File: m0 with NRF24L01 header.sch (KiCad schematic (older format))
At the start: 6 parts

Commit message: Schematic complete
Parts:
- added J?: UART, symbol Connector_Generic:Conn_01x03
- added J?: I2C, symbol Connector_Generic:Conn_01x04
- added J?: ARDU_PINS, symbol Connector:Conn_01x06_Female
- added J?: ARDU_PINS_GND, symbol Connector:Conn_01x06_Female
- added J?: ARDU_PINS_3V3, symbol Connector:Conn_01x06_Female
- added J?: Extra Pins, symbol Connector:Conn_01x07_Female
- added J?: Extra Pins GND, symbol Connector:Conn_01x07_Female
- added J?: Extra Pins 3V3, symbol Connector:Conn_01x07_Female
- added Q?: Q_NMOS_DGS, symbol Device:Q_NMOS_DGS
- added R? (x2): 10k, symbol Device:R
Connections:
- net +3V3: now also J?.1 (Pin_1), J?.1 (Pin_1), J?.1 (Pin_1), J?.2 (Pin_2), J?.2 (Pin_2), J?.3 (Pin_3), J?.3 (Pin_3), J?.4 (Pin_4), J?.4 (Pin_4), J?.5 (Pin_5), J?.5 (Pin_5), J?.6 (Pin_6), J?.6 (Pin_6), J?.7 (Pin_7), Q?.2 (G), R?.1
- net +BATT: now also R?.1
- net GND: now also J?.1 (Pin_1), J?.1 (Pin_1), J?.2 (Pin_2), J?.2 (Pin_2), J?.3 (Pin_3), J?.3 (Pin_3), J?.3 (Pin_3), J?.4 (Pin_4), J?.4 (Pin_4), J?.4 (Pin_4), J?.5 (Pin_5), J?.5 (Pin_5), J?.6 (Pin_6), J?.6 (Pin_6), J?.7 (Pin_7)
- net RX: now also J?.2 (Pin_2)
- net SCL: now also J?.2 (Pin_2)
- net SDA: now also J?.3 (Pin_3)
- net TX: now also J?.1 (Pin_1)
- net Taranis_HEARTBEAT: now also Q?.1 (D), R?.2
- net PWM_TC_INPUT: now reaches Q?.3 (S), R?.2
- new net ARDU_10: J?.2 (Pin_2)
- new net ARDU_12: J?.3 (Pin_3)
- new net ARDU_14: J?.4 (Pin_4)
- new net ARDU_15: J?.5 (Pin_5)
- new net ARDU_19: J?.6 (Pin_6)
- new net ARDU_6: J?.1 (Pin_1)
- new net PA03: J?.1 (Pin_1)
- new net PA21: J?.2 (Pin_2)
- new net PA27: J?.3 (Pin_3)
- new net PA28: J?.4 (Pin_4)
- new net PB03: J?.5 (Pin_5)
- new net PB22: J?.6 (Pin_6)
- new net PB23: J?.7 (Pin_7)
- new net Taranis_HEARTBEAT_3V3: Q?.3 (S), R?.2
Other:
- note added: "Needs to go to timer input"
- note added: "PA07:\nEXTINT[7]\nTCC1(W0)\nTCC3(WO)"
- note added: "To MCU (+VBatt)"
- note added: "To MCU (3.3V)"

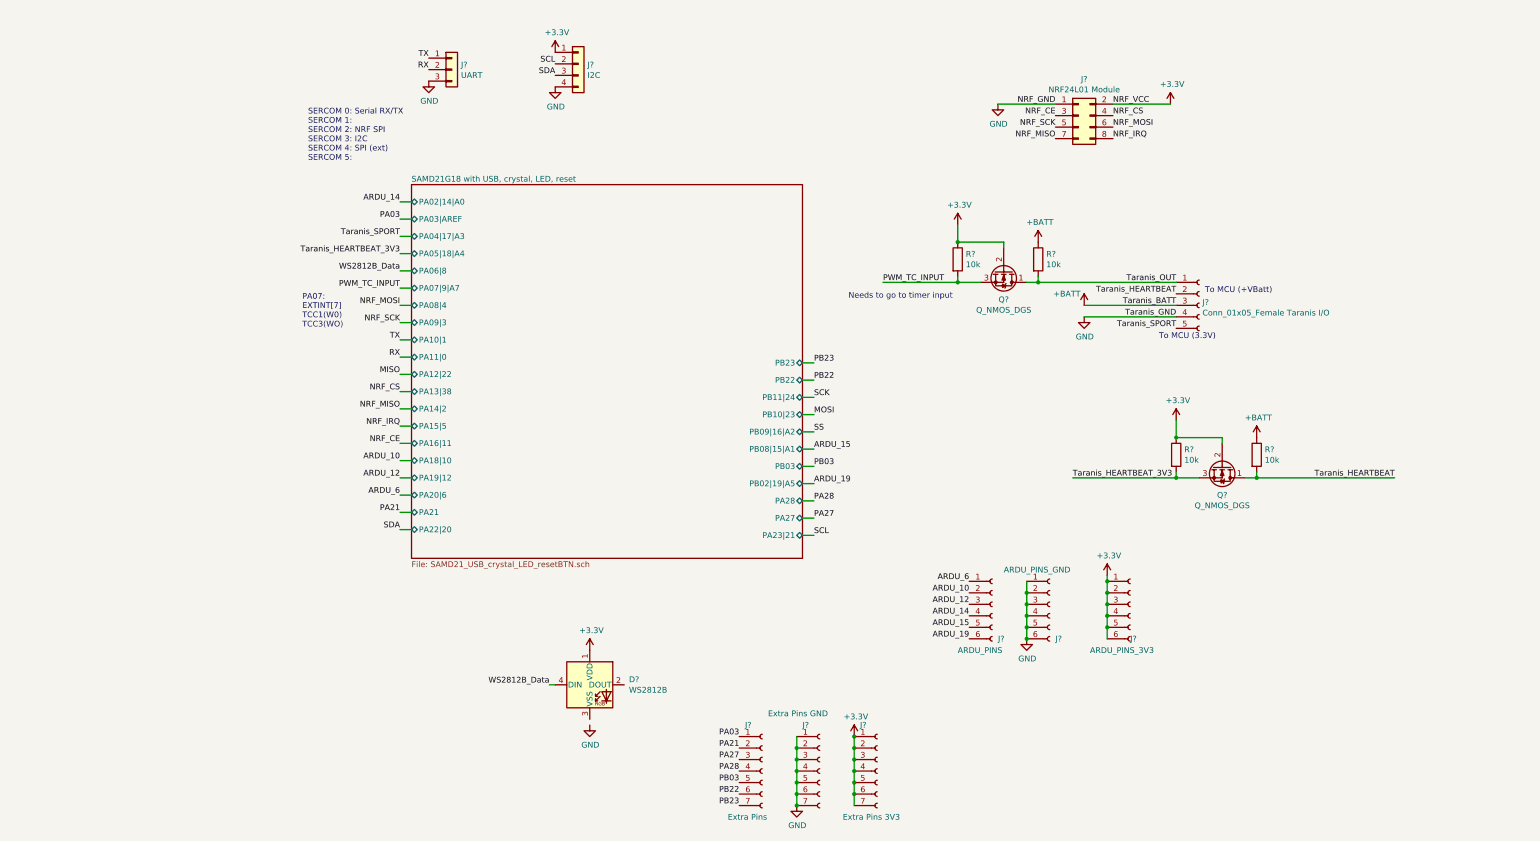
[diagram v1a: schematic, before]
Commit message: Add 3v3 LDO, annotate schematic
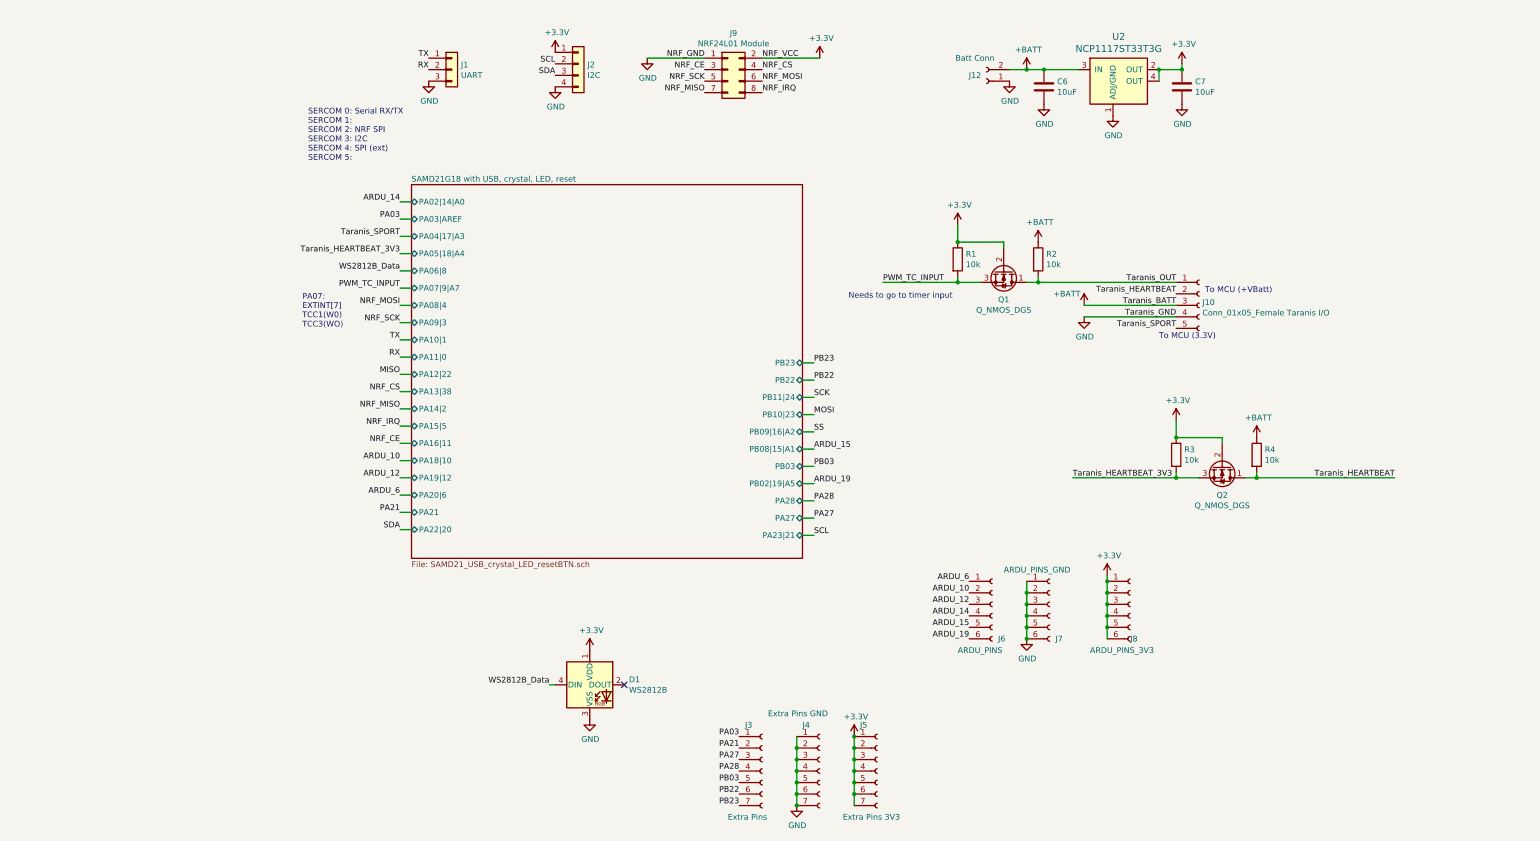
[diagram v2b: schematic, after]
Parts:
- added C6, C7: 10uF, symbol Device:C
- added J12: Batt Conn, symbol Connector:Conn_01x02_Female
- added U2: NCP1117ST33T3G, digikey-footprints:SOT-223, symbol dk_PMIC-Voltage-Regulators-Linear:NCP1117ST33T3G
- gave numbers to parts that had none: 17
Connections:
- net +3V3: now also C7.1, U2.2 (OUT), U2.4 (OUT)
- net +BATT: now also C6.1, J12.2 (Pin_2), U2.3 (IN)
- net GND: now also D1.3 (VSS), C6.2, C7.2, J12.1 (Pin_1), U2.1 (ADJ/GND)
- no-connect marks 0 -> 1
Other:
- moved on the sheet: J9

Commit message: Fix schematic ERC
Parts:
- added D3, D4: D_Schottky, symbol Device:D_Schottky
- added J13: SPI, symbol Connector:Conn_01x06_Female
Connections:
- net +3V3: now also J13.1 (Pin_1)
- net +BATT: now also D3.2 (A); no longer C6.1, U2.3 (IN)
- net GND: now also J13.6 (Pin_6)
- net MISO: now also J13.3 (Pin_3)
- net MOSI: now also J13.2 (Pin_2)
- net SCK: now also J13.4 (Pin_4)
- net SS: now also J13.5 (Pin_5)
- new net: C6.1, D3.1 (K), D4.1 (K), U2.3 (IN)
- new net +5V_USB: D4.2 (A)
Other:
- moved on the sheet: C6, C7, U2

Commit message: XCtal caps changed, all footprints assigned
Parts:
- C6: footprint (none) -> Capacitor_SMD:C_1206_3216Metric
- C7: footprint (none) -> Capacitor_SMD:C_0805_2012Metric; Part (none) -> TPSP106M010R2000
- D3, D4: footprint (none) -> Diode_SMD:D_SMC_Handsoldering
- J1: footprint (none) -> Connector_PinHeader_1.27mm:PinHeader_1x03_P1.27mm_Vertical
- J12: footprint (none) -> Connector_PinHeader_1.27mm:PinHeader_1x02_P1.27mm_Vertical
- J13, J6, J7, J8: footprint (none) -> Connector_PinHeader_1.27mm:PinHeader_1x06_P1.27mm_Vertical
- J2: footprint (none) -> Connector_PinHeader_1.27mm:PinHeader_1x04_P1.27mm_Vertical
- J3, J4, J5: footprint (none) -> Connector_PinHeader_1.27mm:PinHeader_1x07_P1.27mm_Vertical
- J9: footprint (none) -> Connector_PinHeader_1.27mm:PinHeader_2x04_P1.27mm_Vertical
- Q1, Q2: value Q_NMOS_DGS -> SI2304DDS-T1-GE3; footprint (none) -> Package_TO_SOT_SMD:SOT-23
- R1, R2, R3, R4: footprint (none) -> Resistor_SMD:R_0603_1608Metric
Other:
- note added: "ESR: 33mOhm to 2.2Ohm"
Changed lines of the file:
@@
 F 0 "J9" H 4300 1317 50  0000 C CNN
 F 1 "NRF24L01 Module" H 4300 1226 50  0000 C CNN
-F 2 "" H 4250 1000 50  0001 C CNN
+F 2 "Connector_PinHeader_1.27mm:PinHeader_2x04_P1.27mm_Vertical" H 4250 1000 50  0001 C CNN
 F 3 "~" H 4250 1000 50  0001 C CNN
 	1    4250 1000
@@
 P 6650 2750
 F 0 "Q1" V 6900 2750 50  0000 C CNN
-F 1 "Q_NMOS_DGS" V 6991 2750 50  0000 C CNN
-F 2 "" H 6850 2850 50  0001 C CNN
+F 1 "SI2304DDS-T1-GE3" V 6991 2750 50  0000 C CNN
+F 2 "Package_TO_SOT_SMD:SOT-23" H 6850 2850 50  0001 C CNN
 F 3 "~" H 6650 2750 50  0001 C CNN
 	1    6650 2750
@@
 F 0 "R2" H 7020 2696 50  0000 L CNN
 F 1 "10k" H 7020 2605 50  0000 L CNN
-F 2 "" V 6880 2650 50  0001 C CNN
+F 2 "Resistor_SMD:R_0603_1608Metric" V 6880 2650 50  0001 C CNN
 F 3 "~" H 6950 2650 50  0001 C CNN
 	1    6950 2650
@@
 F 0 "R1" H 6320 2696 50  0000 L CNN
 F 1 "10k" H 6320 2605 50  0000 L CNN
-F 2 "" V 6180 2650 50  0001 C CNN
+F 2 "Resistor_SMD:R_0603_1608Metric" V 6180 2650 50  0001 C CNN
 F 3 "~" H 6250 2650 50  0001 C CNN
 	1    6250 2650
@@
 F 0 "J2" H 3030 942 50  0000 L CNN
 F 1 "I2C" H 3030 851 50  0000 L CNN
-F 2 "" H 2950 950 50  0001 C CNN
+F 2 "Connector_PinHeader_1.27mm:PinHeader_1x04_P1.27mm_Vertical" H 2950 950 50  0001 C CNN
 F 3 "~" H 2950 950 50  0001 C CNN
 	1    2950 950
@@
 P 8550 4450
 F 0 "Q2" V 8800 4450 50  0000 C CNN
-F 1 "Q_NMOS_DGS" V 8891 4450 50  0000 C CNN
-F 2 "" H 8750 4550 50  0001 C CNN
+F 1 "SI2304DDS-T1-GE3" V 8891 4450 50  0000 C CNN
+F 2 "Package_TO_SOT_SMD:SOT-23" H 8750 4550 50  0001 C CNN
 F 3 "~" H 8550 4450 50  0001 C CNN
 	1    8550 4450
@@
 F 0 "R4" H 8920 4396 50  0000 L CNN
 F 1 "10k" H 8920 4305 50  0000 L CNN
-F 2 "" V 8780 4350 50  0001 C CNN
+F 2 "Resistor_SMD:R_0603_1608Metric" V 8780 4350 50  0001 C CNN
 F 3 "~" H 8850 4350 50  0001 C CNN
 	1    8850 4350
@@
 F 0 "R3" H 8220 4396 50  0000 L CNN
 F 1 "10k" H 8220 4305 50  0000 L CNN
-F 2 "" V 8080 4350 50  0001 C CNN
+F 2 "Resistor_SMD:R_0603_1608Metric" V 8080 4350 50  0001 C CNN
 F 3 "~" H 8150 4350 50  0001 C CNN
 	1    8150 4350
@@
 F 0 "J6" H 6600 5350 50  0000 L CNN
 F 1 "ARDU_PINS" H 6250 5250 50  0000 L CNN
-F 2 "" H 6550 5650 50  0001 C CNN
+F 2 "Connector_PinHeader_1.27mm:PinHeader_1x06_P1.27mm_Vertical" H 6550 5650 50  0001 C CNN
 F 3 "~" H 6550 5650 50  0001 C CNN
 	1    6550 5650
@@
 F 0 "J7" H 7100 5350 50  0000 L CNN
 F 1 "ARDU_PINS_GND" H 6650 5950 50  0000 L CNN
-F 2 "" H 7050 5650 50  0001 C CNN
+F 2 "Connector_PinHeader_1.27mm:PinHeader_1x06_P1.27mm_Vertical" H 7050 5650 50  0001 C CNN
 F 3 "~" H 7050 5650 50  0001 C CNN
 	1    7050 5650
@@
 F 0 "J8" H 7750 5350 50  0000 L CNN
 F 1 "ARDU_PINS_3V3" H 7400 5250 50  0000 L CNN
-F 2 "" H 7750 5650 50  0001 C CNN
+F 2 "Connector_PinHeader_1.27mm:PinHeader_1x06_P1.27mm_Vertical" H 7750 5650 50  0001 C CNN
 F 3 "~" H 7750 5650 50  0001 C CNN
 	1    7750 5650
@@
 F 0 "J3" H 4400 7500 50  0000 L CNN
 F 1 "Extra Pins" H 4250 6700 50  0000 L CNN
-F 2 "" H 4550 7100 50  0001 C CNN
+F 2 "Connector_PinHeader_1.27mm:PinHeader_1x07_P1.27mm_Vertical" H 4550 7100 50  0001 C CNN
 F 3 "~" H 4550 7100 50  0001 C CNN
 	1    4550 7100
@@
 F 0 "J4" H 4900 7500 50  0000 L CNN
 F 1 "Extra Pins GND" H 4600 7600 50  0000 L CNN
-F 2 "" H 5050 7100 50  0001 C CNN
+F 2 "Connector_PinHeader_1.27mm:PinHeader_1x07_P1.27mm_Vertical" H 5050 7100 50  0001 C CNN
 F 3 "~" H 5050 7100 50  0001 C CNN
 	1    5050 7100
@@
 F 0 "J5" H 5400 7500 50  0000 L CNN
 F 1 "Extra Pins 3V3" H 5250 6700 50  0000 L CNN
-F 2 "" H 5550 7100 50  0001 C CNN
+F 2 "Connector_PinHeader_1.27mm:PinHeader_1x07_P1.27mm_Vertical" H 5550 7100 50  0001 C CNN
 F 3 "~" H 5550 7100 50  0001 C CNN
 	1    5550 7100
@@
 F 0 "J12" H 6600 1050 50  0000 C CNN
 F 1 "Batt Conn" H 6600 900 50  0000 C CNN
-F 2 "" H 6500 1100 50  0001 C CNN
+F 2 "Connector_PinHeader_1.27mm:PinHeader_1x02_P1.27mm_Vertical" H 6500 1100 50  0001 C CNN
 F 3 "~" H 6500 1100 50  0001 C CNN
 	1    6500 1100
@@
 F 0 "C6" H 8015 1196 50  0000 L CNN
 F 1 "10uF" H 8015 1105 50  0000 L CNN
-F 2 "" H 7938 1000 50  0001 C CNN
+F 2 "Capacitor_SMD:C_1206_3216Metric" H 7938 1000 50  0001 C CNN
 F 3 "~" H 7900 1150 50  0001 C CNN
 	1    7900 1150
@@
 F 0 "C7" H 9215 1196 50  0000 L CNN
 F 1 "10uF" H 9215 1105 50  0000 L CNN
-F 2 "" H 9138 1000 50  0001 C CNN
+F 2 "Capacitor_SMD:C_0805_2012Metric" H 9138 1000 50  0001 C CNN
 F 3 "~" H 9100 1150 50  0001 C CNN
+F 4 "TPSP106M010R2000" H 9100 1150 50  0001 C CNN "Part"
 	1    9100 1150
 	1    0    0    -1
@@
 F 0 "J1" H 1930 1042 50  0000 L CNN
 F 1 "UART" H 1930 951 50  0000 L CNN
-F 2 "" H 1850 1000 50  0001 C CNN
+F 2 "Connector_PinHeader_1.27mm:PinHeader_1x03_P1.27mm_Vertical" H 1850 1000 50  0001 C CNN
 F 3 "~" H 1850 1000 50  0001 C CNN
 	1    1850 1000
@@
 F 0 "D3" H 7150 1100 50  0000 C CNN
 F 1 "D_Schottky" H 7150 875 50  0000 C CNN
-F 2 "" H 7150 1000 50  0001 C CNN
+F 2 "Diode_SMD:D_SMC_Handsoldering" H 7150 1000 50  0001 C CNN
 F 3 "~" H 7150 1000 50  0001 C CNN
 	1    7150 1000
@@
 F 0 "D4" H 7500 750 50  0000 C CNN
 F 1 "D_Schottky" H 7500 525 50  0000 C CNN
-F 2 "" H 7500 650 50  0001 C CNN
+F 2 "Diode_SMD:D_SMC_Handsoldering" H 7500 650 50  0001 C CNN
 F 3 "~" H 7500 650 50  0001 C CNN
 	1    7500 650
@@
 F 0 "J13" H 6350 4000 50  0000 L CNN
 F 1 "SPI" H 6350 3900 50  0000 L CNN
-F 2 "" H 6300 4300 50  0001 C CNN
+F 2 "Connector_PinHeader_1.27mm:PinHeader_1x06_P1.27mm_Vertical" H 6300 4300 50  0001 C CNN
 F 3 "~" H 6300 4300 50  0001 C CNN
 	1    6300 4300
@@
 Wire Wire Line
 	8900 1000 8900 1100
+Text Notes 8750 600  0    50   ~ 0
+ESR: 33mOhm to 2.2Ohm
 $EndSCHEMATC

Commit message: Add MCU caps, test points, SWDCLK pull-up; validate ERC and checklist
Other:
- note added: "Expected ERC Error:\nPin 2 (Power Output) should be tied to \nPin 4 (Power Output)"
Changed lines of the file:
@@
 Text Notes 8750 600  0    50   ~ 0
 ESR: 33mOhm to 2.2Ohm
+Text Notes 9400 1100 0    50   ~ 0
+Expected ERC Error:\nPin 2 (Power Output) should be tied to \nPin 4 (Power Output)
 $EndSCHEMATC

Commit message: Change header footprints to 2.54mm
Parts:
- J1: footprint Connector_PinHeader_1.27mm:PinHeader_1x03_P1.27mm_Vertical -> Connector_PinHeader_2.54mm:PinHeader_1x03_P2.54mm_Vertical
- J10: footprint (none) -> Connector_PinHeader_2.54mm:PinHeader_1x05_P2.54mm_Vertical
- J2: footprint Connector_PinHeader_1.27mm:PinHeader_1x04_P1.27mm_Vertical -> Connector_PinHeader_2.54mm:PinHeader_1x04_P2.54mm_Vertical
- J3, J4, J5: footprint Connector_PinHeader_1.27mm:PinHeader_1x07_P1.27mm_Vertical -> Connector_PinHeader_2.54mm:PinHeader_1x07_P2.54mm_Vertical
- J6, J7, J8: footprint Connector_PinHeader_1.27mm:PinHeader_1x06_P1.27mm_Vertical -> Connector_PinHeader_2.54mm:PinHeader_1x06_P2.54mm_Vertical
- J9: footprint Connector_PinHeader_1.27mm:PinHeader_2x04_P1.27mm_Vertical -> Connector_PinHeader_2.54mm:PinHeader_2x04_P2.54mm_Vertical
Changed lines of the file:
@@
 F 0 "J9" H 4300 1317 50  0000 C CNN
 F 1 "NRF24L01 Module" H 4300 1226 50  0000 C CNN
-F 2 "Connector_PinHeader_1.27mm:PinHeader_2x04_P1.27mm_Vertical" H 4250 1000 50  0001 C CNN
+F 2 "Connector_PinHeader_2.54mm:PinHeader_2x04_P2.54mm_Vertical" H 4250 1000 50  0001 C CNN
 F 3 "~" H 4250 1000 50  0001 C CNN
 	1    4250 1000
@@
 F 0 "J10" H 8378 3076 50  0000 L CNN
 F 1 "Conn_01x05_Female Taranis I/O" H 8378 2985 50  0000 L CNN
-F 2 "" H 8350 3050 50  0001 C CNN
+F 2 "Connector_PinHeader_2.54mm:PinHeader_1x05_P2.54mm_Vertical" H 8350 3050 50  0001 C CNN
 F 3 "~" H 8350 3050 50  0001 C CNN
 	1    8350 3050
@@
 F 0 "J2" H 3030 942 50  0000 L CNN
 F 1 "I2C" H 3030 851 50  0000 L CNN
-F 2 "Connector_PinHeader_1.27mm:PinHeader_1x04_P1.27mm_Vertical" H 2950 950 50  0001 C CNN
+F 2 "Connector_PinHeader_2.54mm:PinHeader_1x04_P2.54mm_Vertical" H 2950 950 50  0001 C CNN
 F 3 "~" H 2950 950 50  0001 C CNN
 	1    2950 950
@@
 F 0 "J6" H 6600 5350 50  0000 L CNN
 F 1 "ARDU_PINS" H 6250 5250 50  0000 L CNN
-F 2 "Connector_PinHeader_1.27mm:PinHeader_1x06_P1.27mm_Vertical" H 6550 5650 50  0001 C CNN
+F 2 "Connector_PinHeader_2.54mm:PinHeader_1x06_P2.54mm_Vertical" H 6550 5650 50  0001 C CNN
 F 3 "~" H 6550 5650 50  0001 C CNN
 	1    6550 5650
@@
 F 0 "J7" H 7100 5350 50  0000 L CNN
 F 1 "ARDU_PINS_GND" H 6650 5950 50  0000 L CNN
-F 2 "Connector_PinHeader_1.27mm:PinHeader_1x06_P1.27mm_Vertical" H 7050 5650 50  0001 C CNN
+F 2 "Connector_PinHeader_2.54mm:PinHeader_1x06_P2.54mm_Vertical" H 7050 5650 50  0001 C CNN
 F 3 "~" H 7050 5650 50  0001 C CNN
 	1    7050 5650
@@
 F 0 "J8" H 7750 5350 50  0000 L CNN
 F 1 "ARDU_PINS_3V3" H 7400 5250 50  0000 L CNN
-F 2 "Connector_PinHeader_1.27mm:PinHeader_1x06_P1.27mm_Vertical" H 7750 5650 50  0001 C CNN
+F 2 "Connector_PinHeader_2.54mm:PinHeader_1x06_P2.54mm_Vertical" H 7750 5650 50  0001 C CNN
 F 3 "~" H 7750 5650 50  0001 C CNN
 	1    7750 5650
@@
 F 0 "J3" H 4400 7500 50  0000 L CNN
 F 1 "Extra Pins" H 4250 6700 50  0000 L CNN
-F 2 "Connector_PinHeader_1.27mm:PinHeader_1x07_P1.27mm_Vertical" H 4550 7100 50  0001 C CNN
+F 2 "Connector_PinHeader_2.54mm:PinHeader_1x07_P2.54mm_Vertical" H 4550 7100 50  0001 C CNN
 F 3 "~" H 4550 7100 50  0001 C CNN
 	1    4550 7100
@@
 F 0 "J4" H 4900 7500 50  0000 L CNN
 F 1 "Extra Pins GND" H 4600 7600 50  0000 L CNN
-F 2 "Connector_PinHeader_1.27mm:PinHeader_1x07_P1.27mm_Vertical" H 5050 7100 50  0001 C CNN
+F 2 "Connector_PinHeader_2.54mm:PinHeader_1x07_P2.54mm_Vertical" H 5050 7100 50  0001 C CNN
 F 3 "~" H 5050 7100 50  0001 C CNN
 	1    5050 7100
@@
 F 0 "J5" H 5400 7500 50  0000 L CNN
 F 1 "Extra Pins 3V3" H 5250 6700 50  0000 L CNN
-F 2 "Connector_PinHeader_1.27mm:PinHeader_1x07_P1.27mm_Vertical" H 5550 7100 50  0001 C CNN
+F 2 "Connector_PinHeader_2.54mm:PinHeader_1x07_P2.54mm_Vertical" H 5550 7100 50  0001 C CNN
 F 3 "~" H 5550 7100 50  0001 C CNN
 	1    5550 7100
@@
 F 0 "J1" H 1930 1042 50  0000 L CNN
 F 1 "UART" H 1930 951 50  0000 L CNN
-F 2 "Connector_PinHeader_1.27mm:PinHeader_1x03_P1.27mm_Vertical" H 1850 1000 50  0001 C CNN
+F 2 "Connector_PinHeader_2.54mm:PinHeader_1x03_P2.54mm_Vertical" H 1850 1000 50  0001 C CNN
 F 3 "~" H 1850 1000 50  0001 C CNN
 	1    1850 1000
